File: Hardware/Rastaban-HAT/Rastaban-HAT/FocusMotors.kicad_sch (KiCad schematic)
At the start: 15 parts, among them U6 TMC2208_Carrier, U7 DRV8838 POLOLU, U8 TLV1117-33

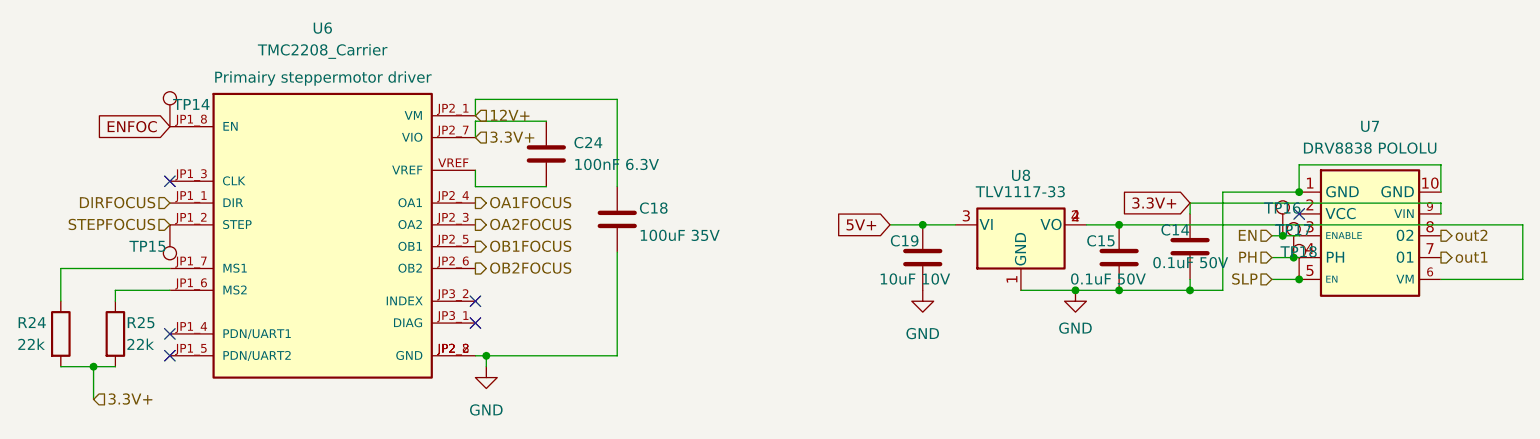
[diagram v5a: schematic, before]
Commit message: changed all capacitor voltages to 50V
This makes ordering and component selection easier.
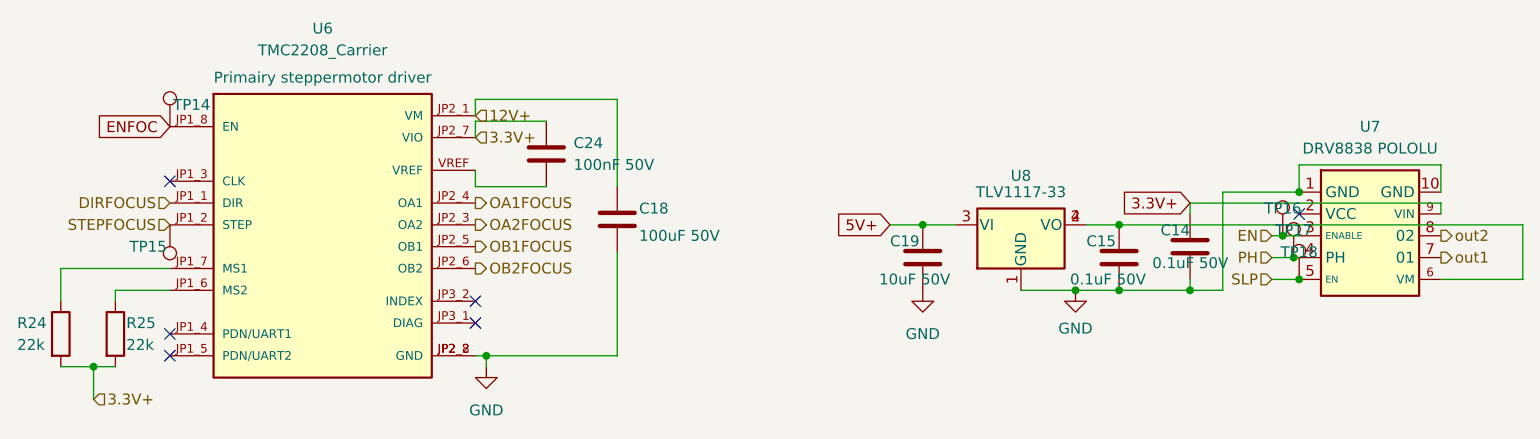
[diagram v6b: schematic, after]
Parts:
- C15: footprint Capacitor_SMD:CP_Elec_6.3x7.7 -> Capacitor_SMD:C_0805_2012Metric_Pad1.18x1.45mm_HandSolder
- C18: value 100uF 35V -> 100uF 50V
- C19: value 10uF 10V -> 10uF 50V
- C24: value 100nF 6.3V -> 100nF 50V
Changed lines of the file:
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@@
       (effects (font (size 1.27 1.27)) (justify right))
     )
-    (property "Footprint" "Capacitor_SMD:CP_Elec_6.3x7.7" (id 2) (at 192.0748 107.315 0)
+    (property "Footprint" "Capacitor_SMD:C_0805_2012Metric_Pad1.18x1.45mm_HandSolder" (id 2) (at 192.0748 107.315 0)
       (effects (font (size 1.27 1.27)) hide)
     )
@@
       (effects (font (size 1.27 1.27)) (justify left))
     )
-    (property "Value" "100uF 35V" (id 1) (at 137.16 108.585 0)
+    (property "Value" "100uF 50V" (id 1) (at 137.16 108.585 0)
       (effects (font (size 1.27 1.27)) (justify left))
     )
@@
       (effects (font (size 1.27 1.27)) (justify left))
     )
-    (property "Value" "100nF 6.3V" (id 1) (at 129.54 100.3299 0)
+    (property "Value" "100nF 50V" (id 1) (at 129.54 100.3299 0)
       (effects (font (size 1.27 1.27)) (justify left))
     )
@@
       (effects (font (size 1.27 1.27)) (justify left))
     )
-    (property "Value" "10uF 10V" (id 1) (at 165.1 113.665 0)
-      (effects (font (size 1.27 1.27)) (justify left))
-    )
+    (property "Value" "10uF 50V" (id 1) (at 165.1 113.665 0)
+      (effects (font (size 1.27 1.27)) (justify left))
+    )

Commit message: changed 0.1ufs to 100nf (more common value)
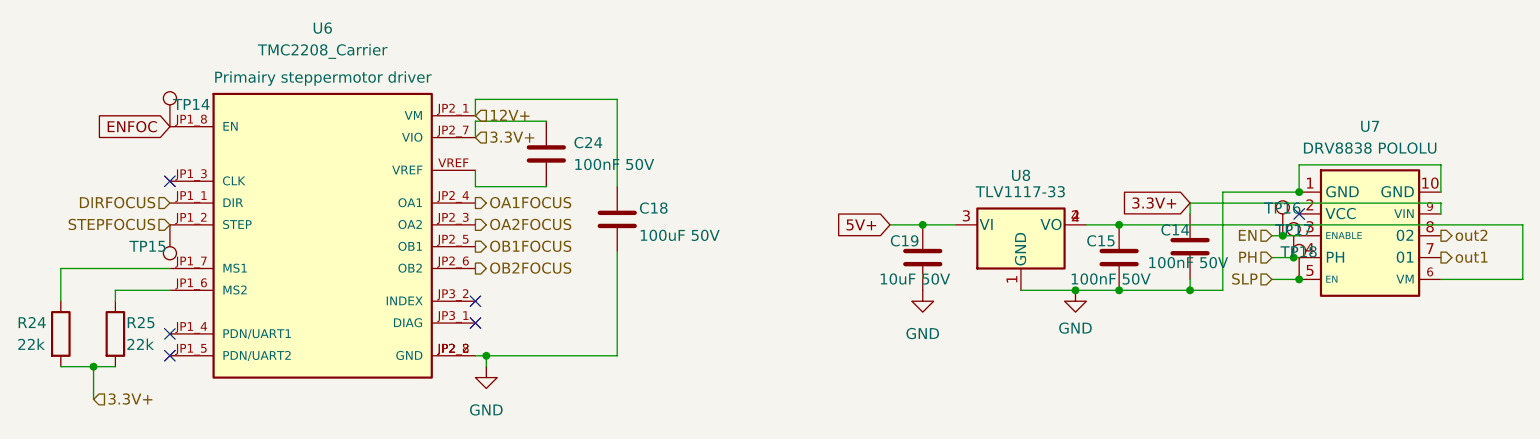
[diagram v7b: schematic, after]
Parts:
- C14, C15: value 0.1uF 50V -> 100nF 50V
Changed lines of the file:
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@@
       (effects (font (size 1.27 1.27)) (justify right))
     )
-    (property "Value" "0.1uF 50V" (id 1) (at 187.325 113.665 0)
+    (property "Value" "100nF 50V" (id 1) (at 187.325 113.665 0)
       (effects (font (size 1.27 1.27)) (justify right))
     )
@@
       (effects (font (size 1.27 1.27)) (justify right))
     )
-    (property "Value" "0.1uF 50V" (id 1) (at 205.74 111.76 0)
+    (property "Value" "100nF 50V" (id 1) (at 205.74 111.76 0)
       (effects (font (size 1.27 1.27)) (justify right))
     )

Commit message: finished BOM file
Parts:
- C14, C15, C24: LCSC (none) -> C531179
- C18: LCSC (none) -> C445063
- C19: footprint Capacitor_SMD:CP_Elec_3x5.4 -> Capacitor_SMD:C_0805_2012Metric_Pad1.18x1.45mm_HandSolder; LCSC (none) -> C17024
- R24, R25: LCSC (none) -> C114565
- TP14, TP15, TP16, TP17, TP18: LCSC (none) -> x; Mouser (none) -> x
- U6: TinyTronics (none) -> https://www.tinytronics.nl/shop/nl/mechanica-en-actuatoren/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
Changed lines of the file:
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@@
+      (effects (font (size 1.27 1.27)) hide)
+    )
+    (property "LCSC" "C531179" (id 5) (at 193.04 111.125 0)
       (effects (font (size 1.27 1.27)) hide)
     )
@@
       (effects (font (size 1.27 1.27)) hide)
     )
+    (property "LCSC" "C531179" (id 5) (at 201.295 109.855 0)
+      (effects (font (size 1.27 1.27)) hide)
+    )
     (pin "1")
     (pin "2")
@@
     )
     (property "Purpose" "decoupling" (id 6) (at 134.62 106.68 0)
+      (effects (font (size 1.27 1.27)) hide)
+    )
+    (property "LCSC" "C445063" (id 7) (at 134.62 106.68 0)
       (effects (font (size 1.27 1.27)) hide)
     )
@@
     )
     (property "Datasheet" "~" (id 3) (at 218.44 111.125 0)
+      (effects (font (size 1.27 1.27)) hide)
+    )
+    (property "LCSC" "x" (id 4) (at 213.36 111.125 0)
+      (effects (font (size 1.27 1.27)) hide)
+    )
+    (property "Mouser" "x" (id 5) (at 213.36 111.125 0)
       (effects (font (size 1.27 1.27)) hide)
     )
@@
     )
     (property "Purpose" "Primairy steppermotor driver" (id 5) (at 100.33 90.17 0))
+    (property "TinyTronics" "https://www.tinytronics.nl/shop/nl/mechanica-en-actuatoren/motoraansturingen-en-drivers/stappen-motoraansturingen-en-drivers/tmc2208-motor-driver-module" (id 6) (at 100.33 109.855 0)
+      (effects (font (size 1.27 1.27)) hide)
+    )
     (pin "JP1_1")
     (pin "JP1_2")
@@
       (effects (font (size 1.27 1.27)) hide)
     )
+    (property "LCSC" "C114565" (id 4) (at 69.85 120.015 0)
+      (effects (font (size 1.27 1.27)) hide)
+    )
     (pin "1")
     (pin "2")
@@
       (effects (font (size 1.27 1.27)) hide)
     )
+    (property "LCSC" "x" (id 4) (at 212.09 108.585 0)
+      (effects (font (size 1.27 1.27)) hide)
+    )
+    (property "Mouser" "x" (id 5) (at 212.09 108.585 0)
+      (effects (font (size 1.27 1.27)) hide)
+    )
     (pin "1")
   )
@@
       (effects (font (size 1.27 1.27)) hide)
     )
+    (property "LCSC" "x" (id 4) (at 82.55 107.315 0)
+      (effects (font (size 1.27 1.27)) hide)
+    )
+    (property "Mouser" "x" (id 5) (at 82.55 107.315 0)
+      (effects (font (size 1.27 1.27)) hide)
+    )
     (pin "1")
   )
@@
     )
     (property "Datasheet" "~" (id 3) (at 87.63 95.885 0)
+      (effects (font (size 1.27 1.27)) hide)
+    )
+    (property "LCSC" "x" (id 4) (at 82.55 95.885 0)
+      (effects (font (size 1.27 1.27)) hide)
+    )
+    (property "Mouser" "x" (id 5) (at 82.55 95.885 0)
       (effects (font (size 1.27 1.27)) hide)
     )
@@
       (effects (font (size 1.27 1.27)) hide)
     )
+    (property "LCSC" "C531179" (id 5) (at 126.365 99.06 0)
+      (effects (font (size 1.27 1.27)) hide)
+    )
     (pin "1")
     (pin "2")
@@
       (effects (font (size 1.27 1.27)) hide)
     )
+    (property "LCSC" "x" (id 4) (at 213.995 113.665 0)
+      (effects (font (size 1.27 1.27)) hide)
+    )
+    (property "Mouser" "x" (id 5) (at 213.995 113.665 0)
+      (effects (font (size 1.27 1.27)) hide)
+    )
     (pin "1")
   )
@@
       (effects (font (size 1.27 1.27)) hide)
     )
+    (property "LCSC" "C114565" (id 4) (at 76.2 120.015 0)
+      (effects (font (size 1.27 1.27)) hide)
+    )
     (pin "1")
     (pin "2")
@@
       (effects (font (size 1.27 1.27)) (justify left))
     )
-    (property "Footprint" "Capacitor_SMD:CP_Elec_3x5.4" (id 2) (at 171.1452 114.935 0)
+    (property "Footprint" "Capacitor_SMD:C_0805_2012Metric_Pad1.18x1.45mm_HandSolder" (id 2) (at 171.1452 114.935 0)
       (effects (font (size 1.27 1.27)) hide)
     )
@@
       (effects (font (size 1.27 1.27)) hide)
     )
+    (property "LCSC" "C17024" (id 7) (at 170.18 111.125 0)
+      (effects (font (size 1.27 1.27)) hide)
+    )
